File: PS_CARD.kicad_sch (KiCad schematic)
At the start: 33 parts, among them J1 430450402, J2 430451602

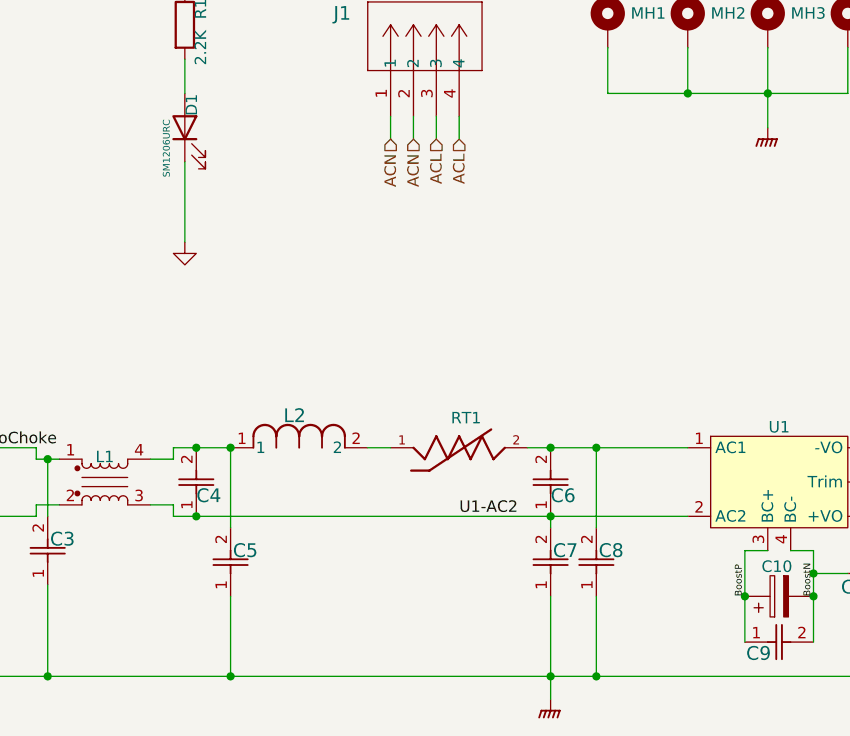
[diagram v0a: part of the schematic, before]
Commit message: Added stiching vias, changed constraints as per MIL275
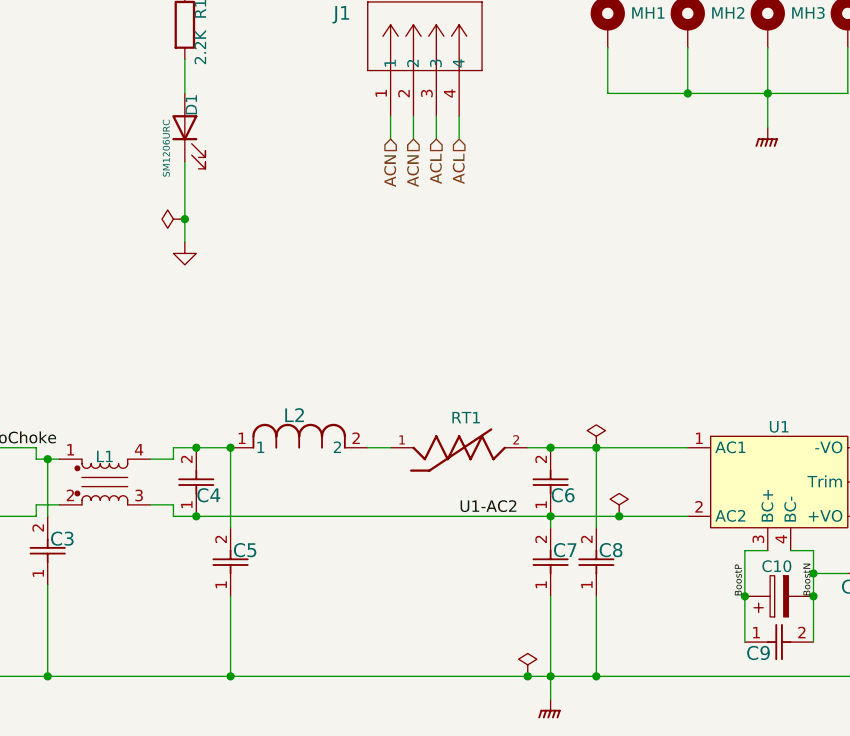
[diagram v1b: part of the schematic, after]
